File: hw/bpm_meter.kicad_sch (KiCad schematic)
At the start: 48 parts, among them J1 Conn_01x06_Pin, Q1 AO3400A, U1 AOZ1282CI, U10 IS31FL3236A, U11 SLS0391FR1A1GD, U12 SLS0391FR1A1GD, U13 SLS0391FR1A1GD, U2 AMS1117-3.3, U3 H11L1

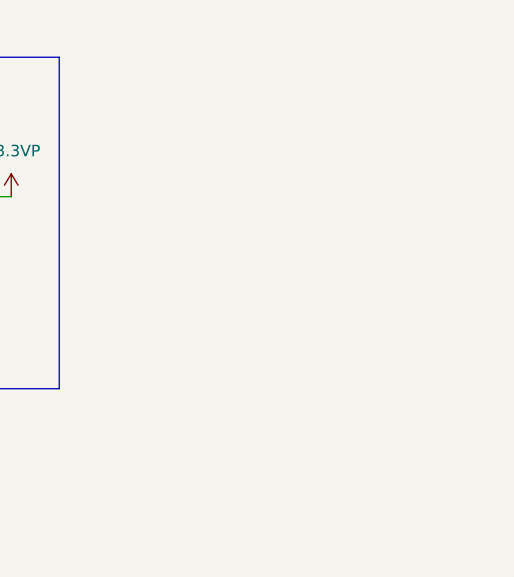
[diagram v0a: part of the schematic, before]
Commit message: Replaced mechanical holder with four M2.5 mounting holes
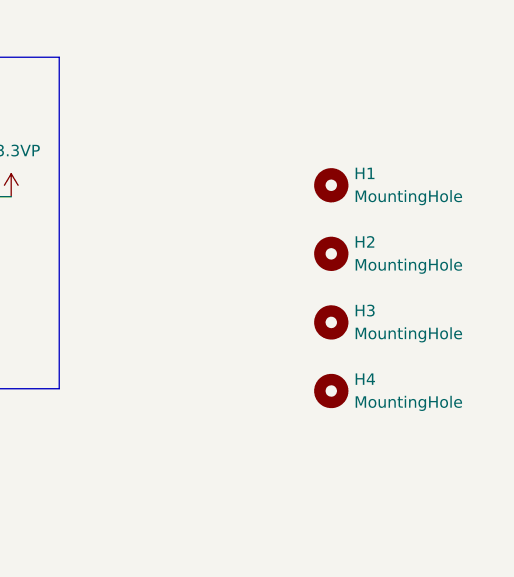
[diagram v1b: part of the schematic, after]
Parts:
- removed HOLDER1: ~, 00_project_library:din_rail_pcb_holder, symbol 00_project_library:din_rail_pcb_holder
- added H1, H2, H3, H4: MountingHole, MountingHole:MountingHole_2.7mm_M2.5, symbol 00_project_library:MountingHole
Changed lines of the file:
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@@
+    )
+  )
+  (symbol (lib_id "00_project_library:MountingHole") (at 264.16 134.62 0) (unit 1)
+    (in_bom yes) (on_board yes) (dnp no) (fields_autoplaced)
+    (property "Reference" "H1" (at 266.7 133.35 0)
+      (effects (font (size 1.27 1.27)) (justify left))
+    )
+    (property "Value" "MountingHole" (at 266.7 135.89 0)
+      (effects (font (size 1.27 1.27)) (justify left))
+    )
+    (property "Footprint" "MountingHole:MountingHole_2.7mm_M2.5" (at 264.16 134.62 0)
+      (effects (font (size 1.27 1.27)) hide)
+    )
+    (property "Datasheet" "~" (at 264.16 134.62 0)
+      (effects (font (size 1.27 1.27)) hide)
+    )
+    (instances
+      (project "bpm_meter"
+        (path "/35c47459-45a7-4753-acae-c8b47e7575e1"
+          (reference "H1") (unit 1)
+        )
+      )
     )
   )
@@
     )
   )
+  (symbol (lib_id "00_project_library:MountingHole") (at 264.16 157.48 0) (unit 1)
+    (in_bom yes) (on_board yes) (dnp no) (fields_autoplaced)
+    (property "Reference" "H4" (at 266.7 156.21 0)
+      (effects (font (size 1.27 1.27)) (justify left))
+    )
+    (property "Value" "MountingHole" (at 266.7 158.75 0)
+      (effects (font (size 1.27 1.27)) (justify left))
+    )
+    (property "Footprint" "MountingHole:MountingHole_2.7mm_M2.5" (at 264.16 157.48 0)
+      (effects (font (size 1.27 1.27)) hide)
+    )
+    (property "Datasheet" "~" (at 264.16 157.48 0)
+      (effects (font (size 1.27 1.27)) hide)
+    )
+    (instances
+      (project "bpm_meter"
+        (path "/35c47459-45a7-4753-acae-c8b47e7575e1"
+          (reference "H4") (unit 1)
+        )
+      )
+    )
+  )
   (symbol (lib_id "Device:R") (at 123.19 64.77 0) (unit 1)
     (in_bom yes) (on_board yes) (dnp no)
@@
         (path "/35c47459-45a7-4753-acae-c8b47e7575e1"
           (reference "C19") (unit 1)
+        )
+      )
+    )
+  )
+  (symbol (lib_id "00_project_library:MountingHole") (at 264.16 149.86 0) (unit 1)
+    (in_bom yes) (on_board yes) (dnp no) (fields_autoplaced)
+    (property "Reference" "H3" (at 266.7 148.59 0)
+      (effects (font (size 1.27 1.27)) (justify left))
+    )
+    (property "Value" "MountingHole" (at 266.7 151.13 0)
+      (effects (font (size 1.27 1.27)) (justify left))
+    )
+    (property "Footprint" "MountingHole:MountingHole_2.7mm_M2.5" (at 264.16 149.86 0)
+      (effects (font (size 1.27 1.27)) hide)
+    )
+    (property "Datasheet" "~" (at 264.16 149.86 0)
+      (effects (font (size 1.27 1.27)) hide)
+    )
+    (instances
+      (project "bpm_meter"
+        (path "/35c47459-45a7-4753-acae-c8b47e7575e1"
+          (reference "H3") (unit 1)
         )
       )
@@
         (path "/35c47459-45a7-4753-acae-c8b47e7575e1"
           (reference "#PWR04") (unit 1)
-        )
-      )
-    )
-  )
-  (symbol (lib_id "00_project_library:din_rail_pcb_holder") (at 177.038 194.818 0) (unit 1)
-    (in_bom no) (on_board yes) (dnp no)
-    (property "Reference" "HOLDER1" (at 30.734 110.998 0)
-      (effects (font (size 1.27 1.27)) (justify left) hide)
-    )
-    (property "Value" "~" (at 177.038 194.818 0)
-      (effects (font (size 1.27 1.27)))
-    )
-    (property "Footprint" "00_project_library:din_rail_pcb_holder" (at 177.038 194.818 0)
-      (effects (font (size 1.27 1.27)) hide)
-    )
-    (property "Datasheet" "" (at 177.038 194.818 0)
-      (effects (font (size 1.27 1.27)) hide)
-    )
-    (instances
-      (project "bpm_meter"
-        (path "/35c47459-45a7-4753-acae-c8b47e7575e1"
-          (reference "HOLDER1") (unit 1)
         )
       )
@@
         )
       )
+    )
+  )
+  (symbol (lib_id "00_project_library:MountingHole") (at 264.16 142.24 0) (unit 1)
+    (in_bom yes) (on_board yes) (dnp no) (fields_autoplaced)
+    (property "Reference" "H2" (at 266.7 140.97 0)
+      (effects (font (size 1.27 1.27)) (justify left))
+    )
+    (property "Value" "MountingHole" (at 266.7 143.51 0)
+      (effects (font (size 1.27 1.27)) (justify left))
+    )
+    (property "Footprint" "MountingHole:MountingHole_2.7mm_M2.5" (at 264.16 142.24 0)
+      (effects (font (size 1.27 1.27)) hide)
+    )
+    (property "Datasheet" "~" (at 264.16 142.24 0)
+      (effects (font (size 1.27 1.27)) hide)
+    )
+    (instances
+      (project "bpm_meter"
+        (path "/35c47459-45a7-4753-acae-c8b47e7575e1"
+          (reference "H2") (unit 1)
+        )
+      )

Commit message: Optimized layout of the RP2040
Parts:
- C1: footprint Diode_SMD:D_1206_3216Metric -> Capacitor_SMD:C_1210_3225Metric
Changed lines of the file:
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@@
       (effects (font (size 1.27 1.27)) (justify left))
     )
-    (property "Footprint" "Diode_SMD:D_1206_3216Metric" (at 127.9652 35.56 0)
+    (property "Footprint" "Capacitor_SMD:C_1210_3225Metric" (at 127.9652 35.56 0)
       (effects (font (size 1.27 1.27)) hide)
     )

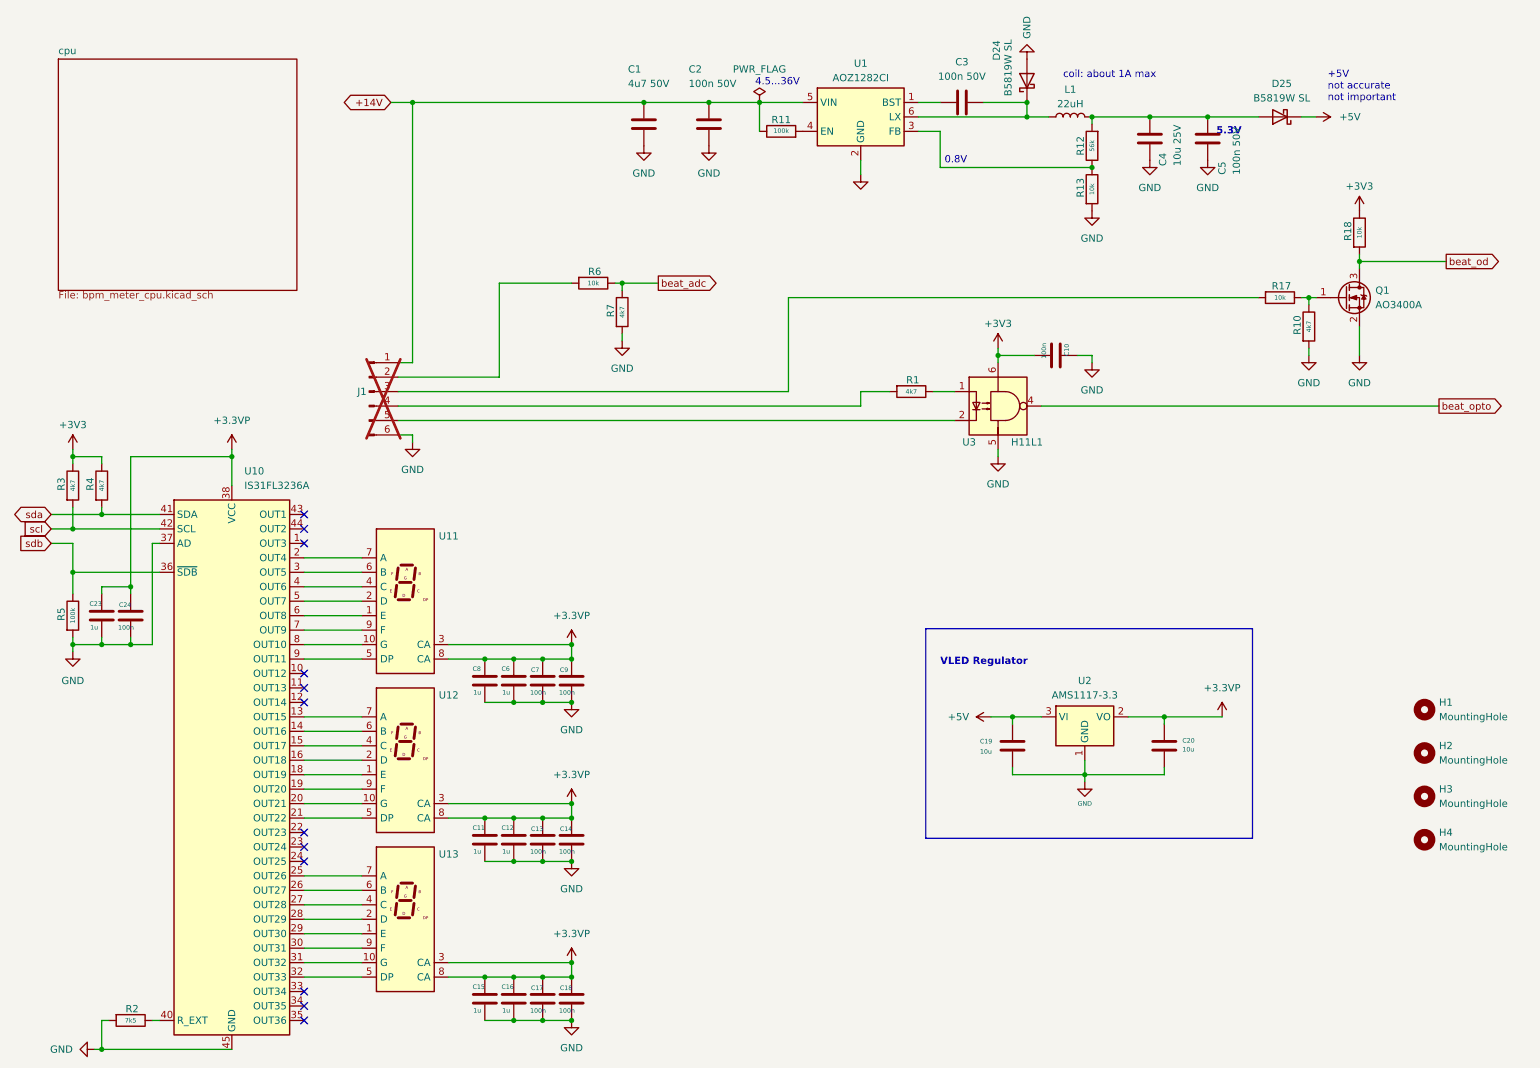
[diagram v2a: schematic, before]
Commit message: Routed part of the design
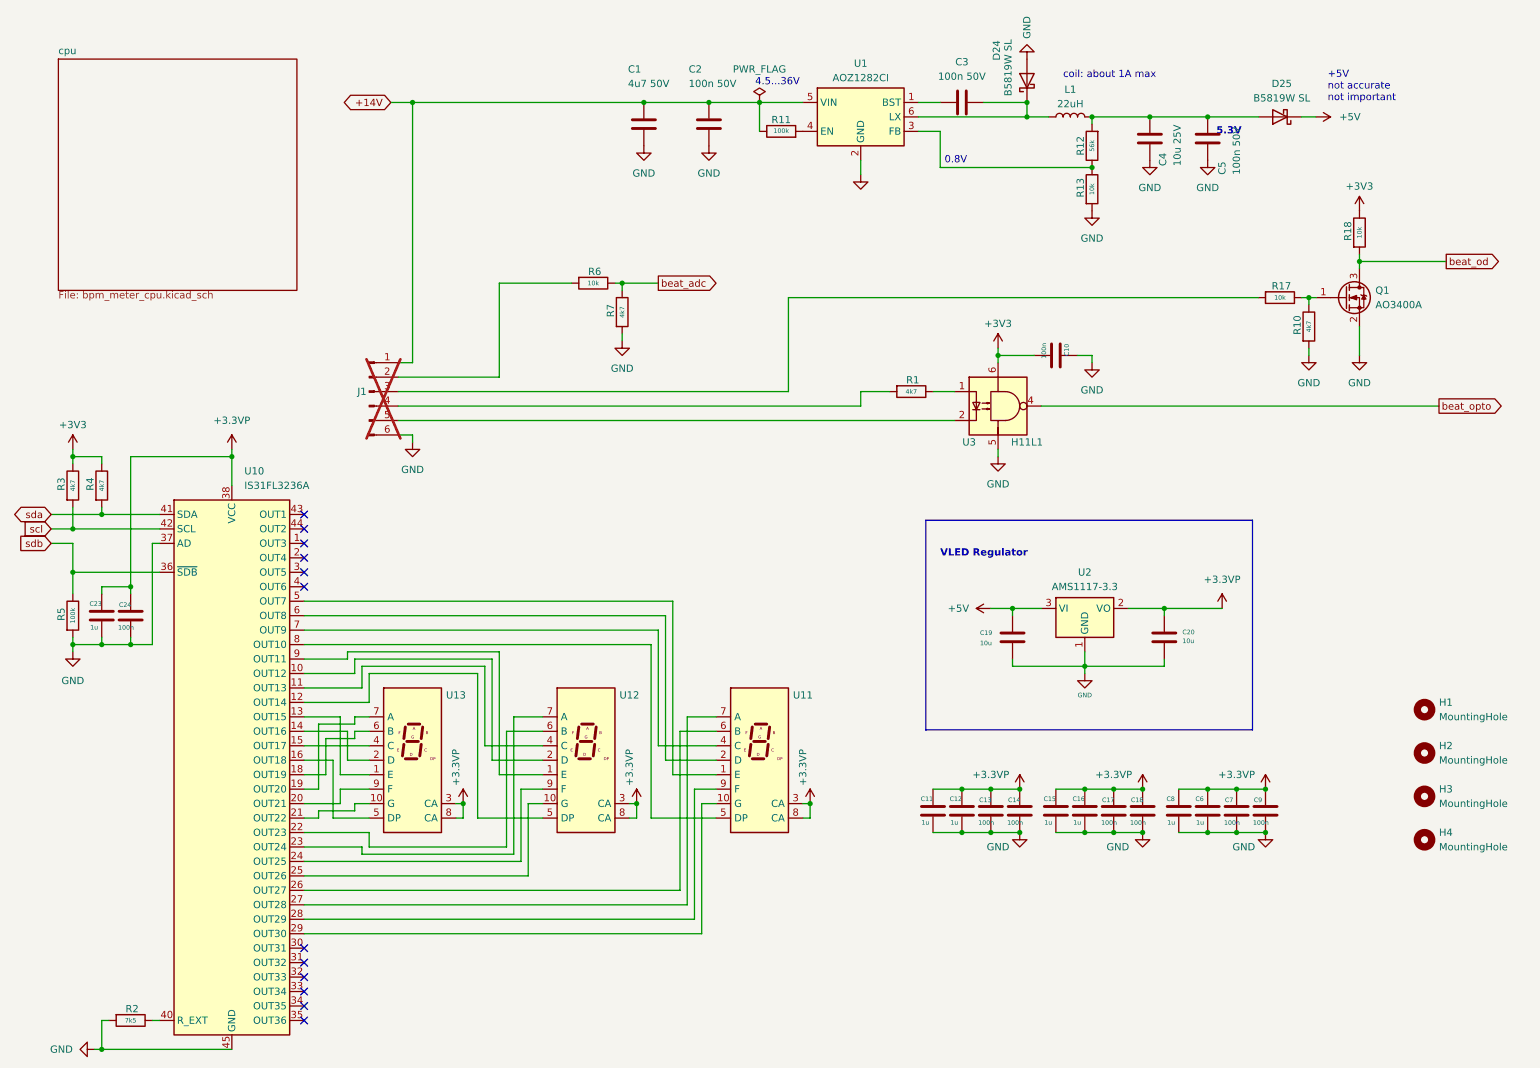
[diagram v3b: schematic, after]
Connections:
- net at U13.1 (E): now also U10.13 (OUT15); no longer U10.29 (OUT30)
- net at U13.10 (G): now also U10.21 (OUT22); no longer U10.31 (OUT32)
- net at U13.2 (D): now also U10.14 (OUT16); no longer U10.28 (OUT29)
- net at U13.4 (C): now also U10.15 (OUT17); no longer U10.27 (OUT28)
- net at U13.5 (DP): now also U10.16 (OUT18); no longer U10.32 (OUT33)
- net at U13.6 (B): now also U10.18 (OUT19); no longer U10.26 (OUT27)
- net at U13.7 (A): now also U10.19 (OUT20); no longer U10.25 (OUT26)
- net at U13.9 (F): now also U10.20 (OUT21); no longer U10.30 (OUT31)
- net at U11.1 (E): now also U10.5 (OUT7); no longer U10.6 (OUT8)
- net at U11.10 (G): now also U10.29 (OUT30); no longer U10.8 (OUT10)
- net at U11.2 (D): now also U10.6 (OUT8); no longer U10.5 (OUT7)
- net at U11.4 (C): now also U10.7 (OUT9); no longer U10.4 (OUT6)
- net at U11.5 (DP): now also U10.8 (OUT10); no longer U10.9 (OUT11)
- net at U11.6 (B): now also U10.26 (OUT27); no longer U10.3 (OUT5)
- net at U11.7 (A): now also U10.27 (OUT28); no longer U10.2 (OUT4)
- net at U11.9 (F): now also U10.28 (OUT29); no longer U10.7 (OUT9)
- net at U10.10 (OUT12): now also U12.2 (D)
- net at U10.11 (OUT13): now also U12.4 (C)
- net at U10.12 (OUT14): now also U12.5 (DP)
- net at U12.7 (A): now also U10.23 (OUT24); no longer U10.13 (OUT15)
- net at U12.6 (B): now also U10.22 (OUT23); no longer U10.14 (OUT16)
- net at U12.1 (E): now also U10.9 (OUT11); no longer U10.18 (OUT19)
- net at U12.9 (F): now also U10.24 (OUT25); no longer U10.19 (OUT20)
- net at U12.10 (G): now also U10.25 (OUT26); no longer U10.20 (OUT21)
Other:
- moved on the sheet: C11, C12, C13, C14, C15, C16, C17, C18, C19, C20, C6, C7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
